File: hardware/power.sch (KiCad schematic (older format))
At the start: 40 parts, among them J1 PowerOut, J13 5V in, U2 PT4103, U4 XC6206P302MR

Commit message: Some routing done
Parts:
- removed C38: 25u 50V, Capacitor_SMD:C_1206_3216Metric, symbol Device:C
- removed C39: 2.2u, Capacitor_SMD:C_0805_2012Metric, symbol Device:C
- removed D1: 1N5819, Diode_SMD:D_SOD-123, symbol Device:D_Schottky
- removed J1: PowerOut, Connector_PinSocket_1.27mm:PinSocket_1x04_P1.27mm_Vertical, symbol Connector_Generic:Conn_01x04
- removed J13: 5V in, Connector_PinSocket_1.27mm:PinSocket_1x02_P1.27mm_Vertical, symbol Connector_Generic:Conn_01x02
- removed L2: 22u, Inductor_SMD:L_Taiyo-Yuden_NR-60xx, symbol Device:L
- removed R23: 5.1, Resistor_SMD:R_0603_1608Metric, symbol Device:R
- removed U2: PT4103, Package_TO_SOT_SMD:SOT-23-6, symbol balmer_allwinner_v3s_v2-rescue:PT4101-balmer
- removed U? (x4): TLV62568DDC or AP3410/SY8008, Package_TO_SOT_SMD:SOT-23-6, symbol Regulator_Switching:TLV62568DDC
- added J13: Conn_01x04, Connector_PinSocket_1.27mm:PinSocket_1x04_P1.27mm_Vertical, symbol Connector_Generic:Conn_01x04
- added J4: USB_C_Receptacle, Connector_USB:USB_C_Receptacle_Amphenol_12401610E4-2A, symbol Connector:USB_C_Receptacle
- added U10, U7, U8, U9: TLV62568DBV, Package_TO_SOT_SMD:SOT-23-5, symbol Regulator_Switching:TLV62568DBV
- R11, R12, R13, R16, R17, R22, R8, R9: renamed from R?; footprint (none) -> Resistor_SMD:R_0603_1608Metric
- gave numbers to parts that had none: 16
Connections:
- net labels removed: VLED+, VLED-
- wire segments 104 -> 76
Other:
- moved on the sheet: C24, C30, C31, C32, C36, C37, C40, C41, C42, C43, C44, C45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

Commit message: More routing. CPU power routed. USB li-ion charging added
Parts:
- removed J13: Conn_01x04, Connector_PinSocket_1.27mm:PinSocket_1x04_P1.27mm_Vertical, symbol Connector_Generic:Conn_01x04
- added C48, C51: 10u, Capacitor_SMD:C_0805_2012Metric, symbol Device:C
- added D4: GRN, LED_SMD:LED_0603_1608Metric, symbol Device:LED
- added D5: RED, LED_SMD:LED_0603_1608Metric, symbol Device:LED
- added J5, J6: Conn_01x01, TestPoint:TestPoint_THTPad_1.0x1.0mm_Drill0.5mm, symbol Connector_Generic:Conn_01x01
- added NTC1: NTCG103UH103JT1, Resistor_SMD:R_0603_1608Metric, symbol Device:R
- added R37, R38: 1R, Resistor_SMD:R_0603_1608Metric, symbol Device:R
- added R39, R40: 1k, Resistor_SMD:R_0603_1608Metric, symbol Device:R
- added R41: 2k, Resistor_SMD:R_0603_1608Metric, symbol Device:R
- added R42: 4k87, Resistor_SMD:R_0603_1608Metric, symbol Device:R
- added R43: 86k6, Resistor_SMD:R_0603_1608Metric, symbol Device:R
- added R44: 0R, Resistor_SMD:R_0603_1608Metric, symbol Device:R
- added U2: TP4056, Package_SO:SOP-8_3.9x4.9mm_P1.27mm, symbol custom:TP4056
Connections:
- net labels added: +BATT
- net labels removed: +5V
- wire segments 76 -> 105
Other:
- moved on the sheet: C24, C30, C31, C32, C36, C37, C40, C41, C42, C43, C44, C45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

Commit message: Power routing done
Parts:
- removed C48, C51: 10u, Capacitor_SMD:C_0805_2012Metric, symbol Device:C
- removed D5: RED, LED_SMD:LED_0603_1608Metric, symbol Device:LED
- removed J5, J6: Conn_01x01, TestPoint:TestPoint_THTPad_1.0x1.0mm_Drill0.5mm, symbol Connector_Generic:Conn_01x01
- removed NTC1: NTCG103UH103JT1, Resistor_SMD:R_0603_1608Metric, symbol Device:R
- removed R38: 1R, Resistor_SMD:R_0603_1608Metric, symbol Device:R
- removed R39, R40: 1k, Resistor_SMD:R_0603_1608Metric, symbol Device:R
- removed R41: 2k, Resistor_SMD:R_0603_1608Metric, symbol Device:R
- removed R42: 4k87, Resistor_SMD:R_0603_1608Metric, symbol Device:R
- removed R43: 86k6, Resistor_SMD:R_0603_1608Metric, symbol Device:R
- removed R44: 0R, Resistor_SMD:R_0603_1608Metric, symbol Device:R
- removed U2: TP4056, Package_SO:SOP-8_3.9x4.9mm_P1.27mm, symbol custom:TP4056
- D4: value GRN -> LED
- R37: value 1R -> 1k
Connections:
- net +BATT is gone; now on net VCC: C24.1, C30.1, C31.1, C32.1, C44.1, C49.1, U10.1 (EN), U10.4 (VIN), U4.3 (VI), U7.1 (EN), U7.4 (VIN), U8.1 (EN), U8.4 (VIN), U9.1 (EN), U9.4 (VIN)
- net GND: now also R37.1
- net VCC: now reaches D4.2 (A)
- net VCC: now also J4.A4 (VBUS), J4.A9 (VBUS), J4.B4 (VBUS), J4.B9 (VBUS); no longer R37.1
- net at D4.1 (K): now also R37.2
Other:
- moved on the sheet: C44

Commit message: Small touch-ups
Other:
- moved on the sheet: J4
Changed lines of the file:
@@
 L Connector:USB_C_Receptacle J4
 U 1 1 6263C86C
-P 1150 2500
-F 0 "J4" H 1257 3767 50  0000 C CNN
-F 1 "USB_C_Receptacle" H 1257 3676 50  0000 C CNN
-F 2 "Connector_USB:USB_C_Receptacle_Amphenol_12401610E4-2A" H 1300 2500 50  0001 C CNN
-F 3 "https://www.usb.org/sites/default/files/documents/usb_type-c.zip" H 1300 2500 50  0001 C CNN
-	1    1150 2500
+P 1150 3000
+F 0 "J4" H 1257 4267 50  0000 C CNN
+F 1 "USB_C_Receptacle" H 1257 4176 50  0000 C CNN
+F 2 "Connector_USB:USB_C_Receptacle_Amphenol_12401610E4-2A" H 1300 3000 50  0001 C CNN
+F 3 "https://www.usb.org/sites/default/files/documents/usb_type-c.zip" H 1300 3000 50  0001 C CNN
+	1    1150 3000
 	1    0    0    -1
 $EndComp
@@
 L power:GND #PWR0138
 U 1 1 626D23B2
-P 1150 4100
-F 0 "#PWR0138" H 1150 3850 50  0001 C CNN
-F 1 "GND" H 1155 3927 50  0001 C CNN
-F 2 "" H 1150 4100 50  0001 C CNN
-F 3 "" H 1150 4100 50  0001 C CNN
-	1    1150 4100
+P 1150 4600
+F 0 "#PWR0138" H 1150 4350 50  0001 C CNN
+F 1 "GND" H 1155 4427 50  0001 C CNN
+F 2 "" H 1150 4600 50  0001 C CNN
+F 3 "" H 1150 4600 50  0001 C CNN
+	1    1150 4600
 	1    0    0    -1
 $EndComp
@@
 L power:GND #PWR0139
 U 1 1 626D2B67
-P 850 4100
-F 0 "#PWR0139" H 850 3850 50  0001 C CNN
-F 1 "GND" H 855 3927 50  0001 C CNN
-F 2 "" H 850 4100 50  0001 C CNN
-F 3 "" H 850 4100 50  0001 C CNN
-	1    850  4100
+P 850 4600
+F 0 "#PWR0139" H 850 4350 50  0001 C CNN
+F 1 "GND" H 855 4427 50  0001 C CNN
+F 2 "" H 850 4600 50  0001 C CNN
+F 3 "" H 850 4600 50  0001 C CNN
+	1    850  4600
 	1    0    0    -1
 $EndComp
@@
 L power:VCC #PWR0140
 U 1 1 625BC204
-P 1750 1500
-F 0 "#PWR0140" H 1750 1350 50  0001 C CNN
-F 1 "VCC" H 1765 1673 50  0000 C CNN
-F 2 "" H 1750 1500 50  0001 C CNN
-F 3 "" H 1750 1500 50  0001 C CNN
-	1    1750 1500
+P 1750 2000
+F 0 "#PWR0140" H 1750 1850 50  0001 C CNN
+F 1 "VCC" H 1765 2173 50  0000 C CNN
+F 2 "" H 1750 2000 50  0001 C CNN
+F 3 "" H 1750 2000 50  0001 C CNN
+	1    1750 2000
 	1    0    0    -1
 $EndComp

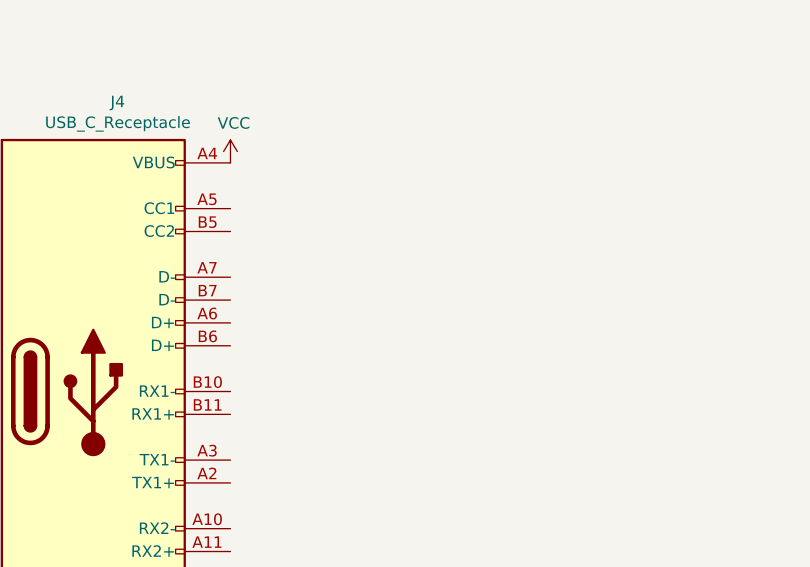
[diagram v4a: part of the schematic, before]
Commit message: Added USB UART
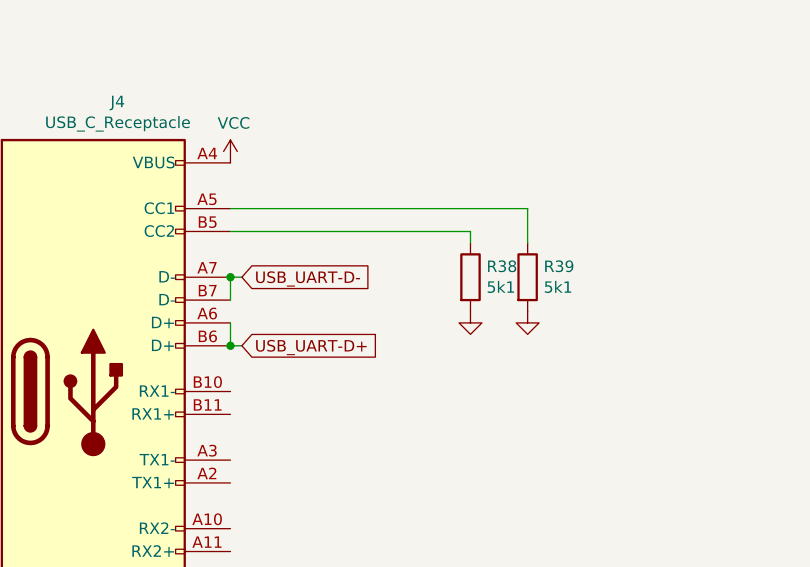
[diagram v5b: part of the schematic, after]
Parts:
- added R38, R39: 5k1, Resistor_SMD:R_0603_1608Metric, symbol Device:R
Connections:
- net GND: now also R38.2, R39.2
- net at J4.A5 (CC1): now also R39.1
- net USB_UART-D+: now reaches J4.A6 (D+)
- net USB_UART-D+: now also J4.B6 (D+)
- net USB_UART-D-: now reaches J4.A7 (D-)
- net USB_UART-D-: now also J4.B7 (D-)
- net at J4.B5 (CC2): now also R38.1
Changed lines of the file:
@@
 	1    0    0    -1
 $EndComp
+Wire Wire Line
+	2800 2300 2800 2350
+$Comp
+L Device:R R39
+U 1 1 62831F6F
+P 3050 2500
+F 0 "R39" H 3120 2546 50  0000 L CNN
+F 1 "5k1" H 3120 2455 50  0000 L CNN
+F 2 "Resistor_SMD:R_0603_1608Metric" V 2980 2500 50  0001 C CNN
+F 3 "~" H 3050 2500 50  0001 C CNN
+	1    3050 2500
+	1    0    0    -1
+$EndComp
+$Comp
+L Device:R R38
+U 1 1 62831656
+P 2800 2500
+F 0 "R38" H 2870 2546 50  0000 L CNN
+F 1 "5k1" H 2870 2455 50  0000 L CNN
+F 2 "Resistor_SMD:R_0603_1608Metric" V 2730 2500 50  0001 C CNN
+F 3 "~" H 2800 2500 50  0001 C CNN
+	1    2800 2500
+	1    0    0    -1
+$EndComp
+Wire Wire Line
+	3050 2200 3050 2350
+$Comp
+L power:GND #PWR027
+U 1 1 6283D01F
+P 2800 2650
+F 0 "#PWR027" H 2800 2400 50  0001 C CNN
+F 1 "GND" H 2805 2477 50  0001 C CNN
+F 2 "" H 2800 2650 50  0001 C CNN
+F 3 "" H 2800 2650 50  0001 C CNN
+	1    2800 2650
+	1    0    0    -1
+$EndComp
+$Comp
+L power:GND #PWR028
+U 1 1 6283D4A2
+P 3050 2650
+F 0 "#PWR028" H 3050 2400 50  0001 C CNN
+F 1 "GND" H 3055 2477 50  0001 C CNN
+F 2 "" H 3050 2650 50  0001 C CNN
+F 3 "" H 3050 2650 50  0001 C CNN
+	1    3050 2650
+	1    0    0    -1
+$EndComp
+Text GLabel 1800 2800 2    50   Input ~ 0
+USB_UART-D+
+Text GLabel 1800 2500 2    50   Input ~ 0
+USB_UART-D-
+Wire Wire Line
+	1750 2200 3050 2200
+Wire Wire Line
+	1750 2300 2800 2300
+Wire Wire Line
+	1750 2600 1750 2500
+Wire Wire Line
+	1750 2500 1800 2500
+Connection ~ 1750 2500
+Wire Wire Line
+	1750 2700 1750 2800
+Wire Wire Line
+	1750 2800 1800 2800
+Connection ~ 1750 2800
 $EndSCHEMATC

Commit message: 0R between VBus and VCC
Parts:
- added R30: 0, Resistor_SMD:R_0603_1608Metric, symbol Device:R
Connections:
- net VCC: now also R30.2; no longer J4.A4 (VBUS), J4.A9 (VBUS), J4.B4 (VBUS), J4.B9 (VBUS)
- new net: J4.A4 (VBUS), J4.A9 (VBUS), J4.B4 (VBUS), J4.B9 (VBUS), R30.1
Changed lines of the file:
@@
 L power:VCC #PWR0140
 U 1 1 625BC204
-P 1750 2000
-F 0 "#PWR0140" H 1750 1850 50  0001 C CNN
-F 1 "VCC" H 1765 2173 50  0000 C CNN
-F 2 "" H 1750 2000 50  0001 C CNN
-F 3 "" H 1750 2000 50  0001 C CNN
-	1    1750 2000
+P 2050 2000
+F 0 "#PWR0140" H 2050 1850 50  0001 C CNN
+F 1 "VCC" H 2065 2173 50  0000 C CNN
+F 2 "" H 2050 2000 50  0001 C CNN
+F 3 "" H 2050 2000 50  0001 C CNN
+	1    2050 2000
 	1    0    0    -1
 $EndComp
@@
 	1750 2800 1800 2800
 Connection ~ 1750 2800
+$Comp
+L Device:R R30
+U 1 1 622758D2
+P 1900 2000
+F 0 "R30" V 2000 2000 50  0000 C CNN
+F 1 "0" V 1900 2000 50  0000 C CNN
+F 2 "Resistor_SMD:R_0603_1608Metric" V 1830 2000 50  0001 C CNN
+F 3 "~" H 1900 2000 50  0001 C CNN
+	1    1900 2000
+	0    -1   -1   0
+$EndComp
 $EndSCHEMATC

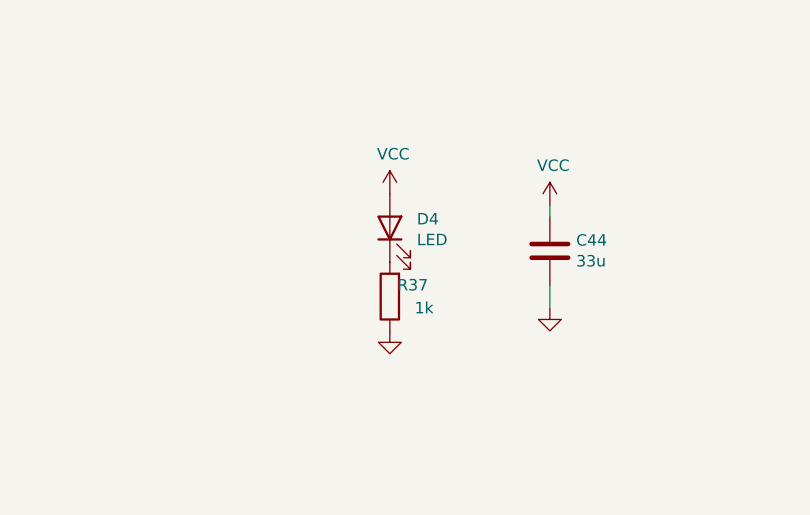
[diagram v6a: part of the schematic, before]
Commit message: Added an "RDY" LED
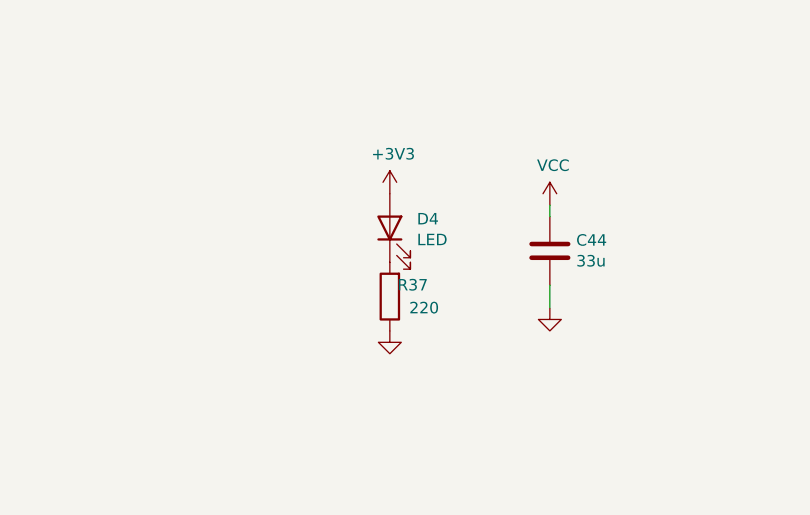
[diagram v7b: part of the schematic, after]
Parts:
- R37: value 1k -> 220
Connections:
- net +3V3: now also D4.2 (A)
- net VCC: no longer D4.2 (A)
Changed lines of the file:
@@
-$EndComp
-$Comp
-L power:VCC #PWR07
-U 1 1 625E2B58
-P 5050 1450
-F 0 "#PWR07" H 5050 1300 50  0001 C CNN
-F 1 "VCC" H 5065 1623 50  0000 C CNN
-F 2 "" H 5050 1450 50  0001 C CNN
-F 3 "" H 5050 1450 50  0001 C CNN
-	1    5050 1450
-	1    0    0    -1
 $EndComp
 $Comp
@@
 P 5050 1900
 F 0 "R37" H 4950 1850 50  0000 C CNN
-F 1 "1k" H 4900 1950 50  0000 C CNN
+F 1 "220" H 4900 1950 50  0000 C CNN
 F 2 "Resistor_SMD:R_0603_1608Metric" V 4980 1900 50  0001 C CNN
 F 3 "~" H 5050 1900 50  0001 C CNN
@@
 	0    -1   -1   0
 $EndComp
+$Comp
+L power:+3V3 #PWR?
+U 1 1 6231043D
+P 5050 1450
+F 0 "#PWR?" H 5050 1300 50  0001 C CNN
+F 1 "+3V3" H 5065 1623 50  0000 C CNN
+F 2 "" H 5050 1450 50  0001 C CNN
+F 3 "" H 5050 1450 50  0001 C CNN
+	1    5050 1450
+	1    0    0    -1
+$EndComp
 $EndSCHEMATC
